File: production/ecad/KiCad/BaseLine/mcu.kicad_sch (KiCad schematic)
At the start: 45 parts, among them J2 1332645, Q1 AO3400A, Q2 AO3400A, SW1 SW_Push, SW2 SW_Push, U2 ESP32-WROOM-32UE_M113EH6400UH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, U3 CP2102N-A02-GQFN28

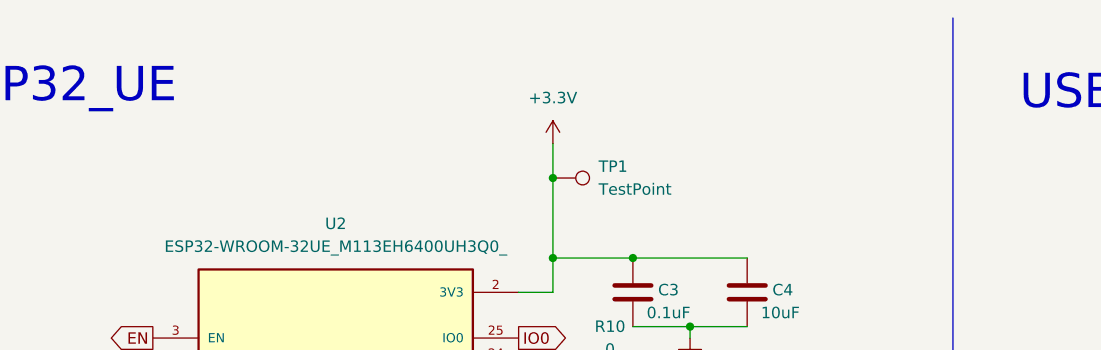
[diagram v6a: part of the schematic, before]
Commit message: Added some footprints and changed push button
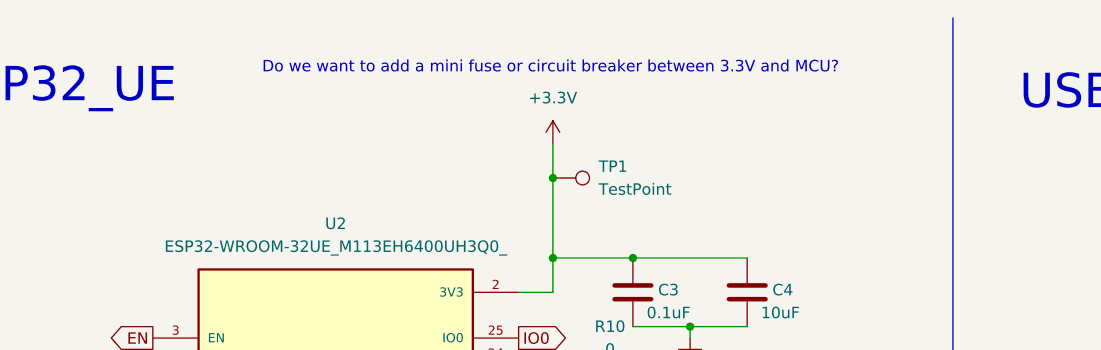
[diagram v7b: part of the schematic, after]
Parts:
- C3, C4, C6, C7: footprint (none) -> Capacitor_SMD:C_0805_2012Metric
- R10, R12, R13, R14, R15, R16, R17, R18, R20, R21, R23, R24, R25, R26, R27, R28, R29, R41, R6, R7: footprint (none) -> Resistor_SMD:R_0805_2012Metric
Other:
- note added: "Do we want to add a mini fuse or circuit breaker between 3.3V and MCU?"
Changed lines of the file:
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@@
 		)
 	)
+	(text "Do we want to add a mini fuse or circuit breaker between 3.3V and MCU?\n"
+		(exclude_from_sim no)
+		(at 86.106 18.288 0)
+		(effects
+			(font
+				(size 1.27 1.27)
+			)
+		)
+	)
 	(text "Reset Button\n"
 		(exclude_from_sim no)
@@
 			)
 		)
-		(property "Footprint" ""
+		(property "Footprint" "Resistor_SMD:R_0805_2012Metric"
 			(at 168.91 76.2 0)
 			(effects
@@
 			)
 		)
-		(property "Footprint" ""
+		(property "Footprint" "Capacitor_SMD:C_0805_2012Metric"
 			(at 96.2152 46.99 0)
 			(effects
@@
 			)
 		)
-		(property "Footprint" ""
+		(property "Footprint" "Resistor_SMD:R_0805_2012Metric"
 			(at 106.68 85.598 90)
 			(effects
@@
 			)
 		)
-		(property "Footprint" ""
+		(property "Footprint" "Resistor_SMD:R_0805_2012Metric"
 			(at 252.73 52.578 90)
 			(effects
@@
 			)
 		)
-		(property "Footprint" ""
+		(property "Footprint" "Resistor_SMD:R_0805_2012Metric"
 			(at 106.68 72.898 90)
 			(effects
@@
 			)
 		)
-		(property "Footprint" ""
+		(property "Footprint" "Resistor_SMD:R_0805_2012Metric"
 			(at 252.73 55.118 90)
 			(effects
@@
 			)
 		)
-		(property "Footprint" ""
+		(property "Footprint" "Resistor_SMD:R_0805_2012Metric"
 			(at 190.5 130.302 90)
 			(effects
@@
 			)
 		)
-		(property "Footprint" ""
+		(property "Footprint" "Resistor_SMD:R_0805_2012Metric"
 			(at 252.73 62.738 90)
 			(effects
@@
 			)
 		)
-		(property "Footprint" ""
+		(property "Footprint" "Resistor_SMD:R_0805_2012Metric"
 			(at 92.71 55.118 90)
 			(effects
@@
 			)
 		)
-		(property "Footprint" ""
+		(property "Footprint" "Resistor_SMD:R_0805_2012Metric"
 			(at 106.68 98.298 90)
 			(effects
@@
 			)
 		)
-		(property "Footprint" ""
+		(property "Footprint" "Resistor_SMD:R_0805_2012Metric"
 			(at 106.68 95.758 90)
 			(effects
@@
 			)
 		)
-		(property "Footprint" ""
+		(property "Footprint" "Resistor_SMD:R_0805_2012Metric"
 			(at 251.46 71.12 0)
 			(effects
@@
 			)
 		)
-		(property "Footprint" ""
+		(property "Footprint" "Resistor_SMD:R_0805_2012Metric"
 			(at 26.67 77.978 90)
 			(effects
@@
 			)
 		)
-		(property "Footprint" ""
+		(property "Footprint" "Resistor_SMD:R_0805_2012Metric"
 			(at 246.38 68.58 0)
 			(effects
@@
 			)
 		)
-		(property "Footprint" ""
+		(property "Footprint" "Resistor_SMD:R_0805_2012Metric"
 			(at 26.67 80.518 90)
 			(effects
@@
 			)
 		)
-		(property "Footprint" ""
+		(property "Footprint" "Capacitor_SMD:C_0805_2012Metric"
 			(at 262.5852 41.91 0)
 			(effects
@@
 			)
 		)
-		(property "Footprint" ""
+		(property "Footprint" "Resistor_SMD:R_0805_2012Metric"
 			(at 106.68 70.358 90)
 			(effects
@@
 			)
 		)
-		(property "Footprint" ""
+		(property "Footprint" "Resistor_SMD:R_0805_2012Metric"
 			(at 246.38 133.35 0)
 			(effects
@@
 			)
 		)
-		(property "Footprint" ""
+		(property "Footprint" "Capacitor_SMD:C_0805_2012Metric"
 			(at 108.9152 46.99 0)
 			(effects
@@
 			)
 		)
-		(property "Footprint" ""
+		(property "Footprint" "Resistor_SMD:R_0805_2012Metric"
 			(at 106.68 80.518 90)
 			(effects
@@
 			)
 		)
-		(property "Footprint" ""
+		(property "Footprint" "Capacitor_SMD:C_0805_2012Metric"
 			(at 248.6152 41.91 0)
 			(effects
@@
 			)
 		)
-		(property "Footprint" ""
+		(property "Footprint" "Resistor_SMD:R_0805_2012Metric"
 			(at 106.68 60.198 90)
 			(effects
@@
 			)
 		)
-		(property "Footprint" ""
+		(property "Footprint" "Resistor_SMD:R_0805_2012Metric"
 			(at 190.5 41.91 0)
 			(effects
@@
 			)
 		)
-		(property "Footprint" ""
+		(property "Footprint" "Resistor_SMD:R_0805_2012Metric"
 			(at 168.91 66.04 0)
 			(effects

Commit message: Rohi changes
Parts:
- removed R28, R29: 0, Resistor_SMD:R_0805_2012Metric, symbol Device:R
- added R47, R48: 4.7k, Resistor_SMD:R_0805_2012Metric, symbol Device:R
- R27: value 0 -> 4.7k
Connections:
- net +3.3V: now also R11.2, R47.2, R48.2; no longer R11.1
- net EN: now also R11.1; no longer R11.2
- net GND: now also R27.2
- net SCL: now also R48.1
- net SDA: now also R47.1
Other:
- note removed: "Do we want to add a mini fuse or circuit breaker between 3.3V and MCU?"
- moved on the sheet: C2, C5, Q1, Q2, R11, R19, R23, R27, R8, R9, SW1, SW2
